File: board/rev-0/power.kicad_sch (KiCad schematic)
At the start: 25 parts, among them J8 S2B-PH-K-SLFSN, U8 BQ24075RGT, U9 TPS62132

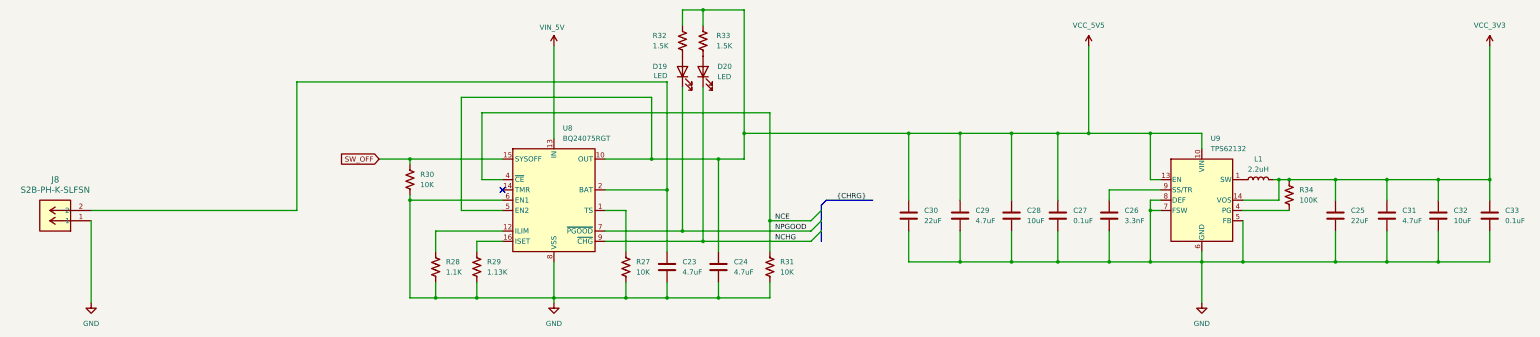
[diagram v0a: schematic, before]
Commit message: First crack at layout, added scottokeebs 3d files
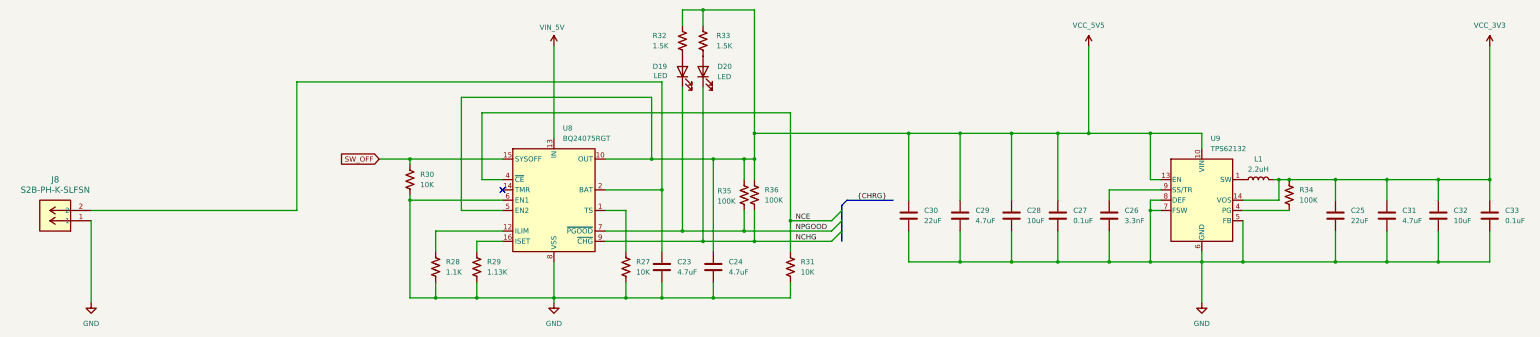
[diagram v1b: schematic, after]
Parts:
- added R35, R36: 100K, Resistor_SMD:R_0603_1608Metric, symbol Device:R_US
- C23, C24, C25, C26, C27, C28, C29, C30, C31, C32, C33: footprint (none) -> Capacitor_SMD:C_0603_1608Metric
- D19, D20: footprint (none) -> LED_SMD:LED_0603_1608Metric
- J8: footprint CONN_S2B-PH-K-S_JST -> Connector_JST:JST_PH_S2B-PH-K_1x02_P2.00mm_Horizontal
- L1: footprint (none) -> Inductor_SMD:L_0805_2012Metric
- R27, R28, R29, R30, R31, R32, R33, R34: footprint (none) -> Resistor_SMD:R_0603_1608Metric
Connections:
- net NCHG: now also R36.2
- net NPGOOD: now also R35.2
- net VCC_5V5: now also R35.1, R36.1
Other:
- moved on the sheet: C23, C24, R31

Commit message: Added battery divider to ADC, created board step file, updated to kicad 9
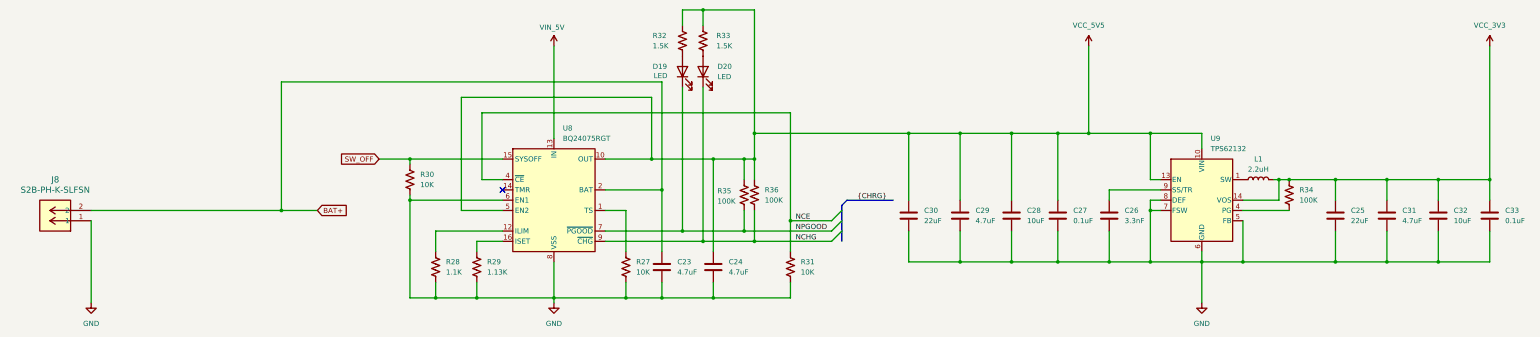
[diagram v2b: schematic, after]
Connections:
- net BAT+: now reaches C23.1, J8.2, U8.2 (BAT), U8.3 (BAT)
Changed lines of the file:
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@@
 (kicad_sch
-	(version 20231120)
+	(version 20250114)
 	(generator "eeschema")
-	(generator_version "8.0")
+	(generator_version "9.0")
 	(paper "C")
 	(title_block
@@
 	)
 	(junction
+		(at 161.29 205.74)
+		(diameter 0)
+		(color 0 0 0 0)
+	)
+	(junction
 		(at 410.21 198.12)
 		(diameter 0)
@@
 	(wire
 		(pts
-			(xy 165.1 173.99) (xy 255.27 173.99)
+			(xy 161.29 173.99) (xy 255.27 173.99)
 		)
 		(stroke
@@
 	(wire
 		(pts
+			(xy 161.29 205.74) (xy 170.18 205.74)
+		)
+		(stroke
+			(width 0)
+			(type default)
+		)
+	)
+	(wire
+		(pts
 			(xy 210.82 181.61) (xy 287.02 181.61)
 		)
@@
 	(wire
 		(pts
-			(xy 114.3 205.74) (xy 165.1 205.74)
+			(xy 114.3 205.74) (xy 161.29 205.74)
 		)
 		(stroke
@@
 	(wire
 		(pts
-			(xy 165.1 205.74) (xy 165.1 173.99)
+			(xy 161.29 205.74) (xy 161.29 173.99)
 		)
 		(stroke
@@
 		)
 	)
+	(global_label "BAT+"
+		(shape input)
+		(at 170.18 205.74 0)
+		(fields_autoplaced yes)
+		(effects
+			(font
+				(size 1.27 1.27)
+			)
+			(justify left)
+		)
+		(property "Intersheetrefs" "${INTERSHEET_REFS}"
+			(at 178.0638 205.74 0)
+			(effects
+				(font
+					(size 1.27 1.27)
+				)
+				(justify left)
+				(hide yes)
+			)
+		)
+	)
